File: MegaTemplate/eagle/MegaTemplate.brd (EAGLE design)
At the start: 160 x 100 mm, 7 parts

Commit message: Template for Arduino Mega Shields
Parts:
- moved SV6 52.5 mm to (30.5, 50.8)
- moved SV2 52.4 mm to (59.7, 2.54)
- moved SV3 44.4 mm to (82.5, 2.54)
- moved SV5 27.0 mm to (54.6, 50.8)
- moved SV7 18.3 mm to (95.2, 29.2), turned to 90 degrees
- moved SV4 13.7 mm to (77.5, 50.8)
- moved SV1 5.24 mm to (36.8, 2.54)
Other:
- board size 160 x 100 mm -> 101.6 x 53.3 mm

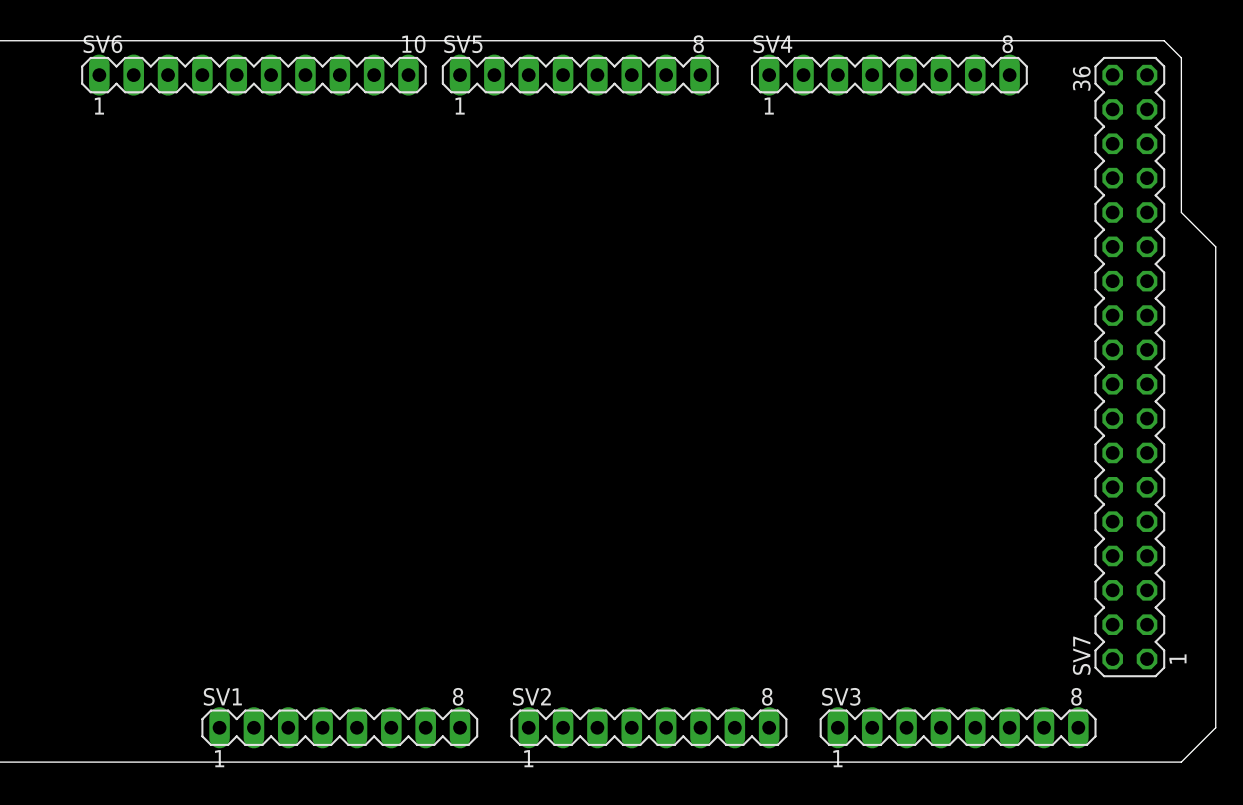
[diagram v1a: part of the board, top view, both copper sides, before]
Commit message: fixed pin header orientation
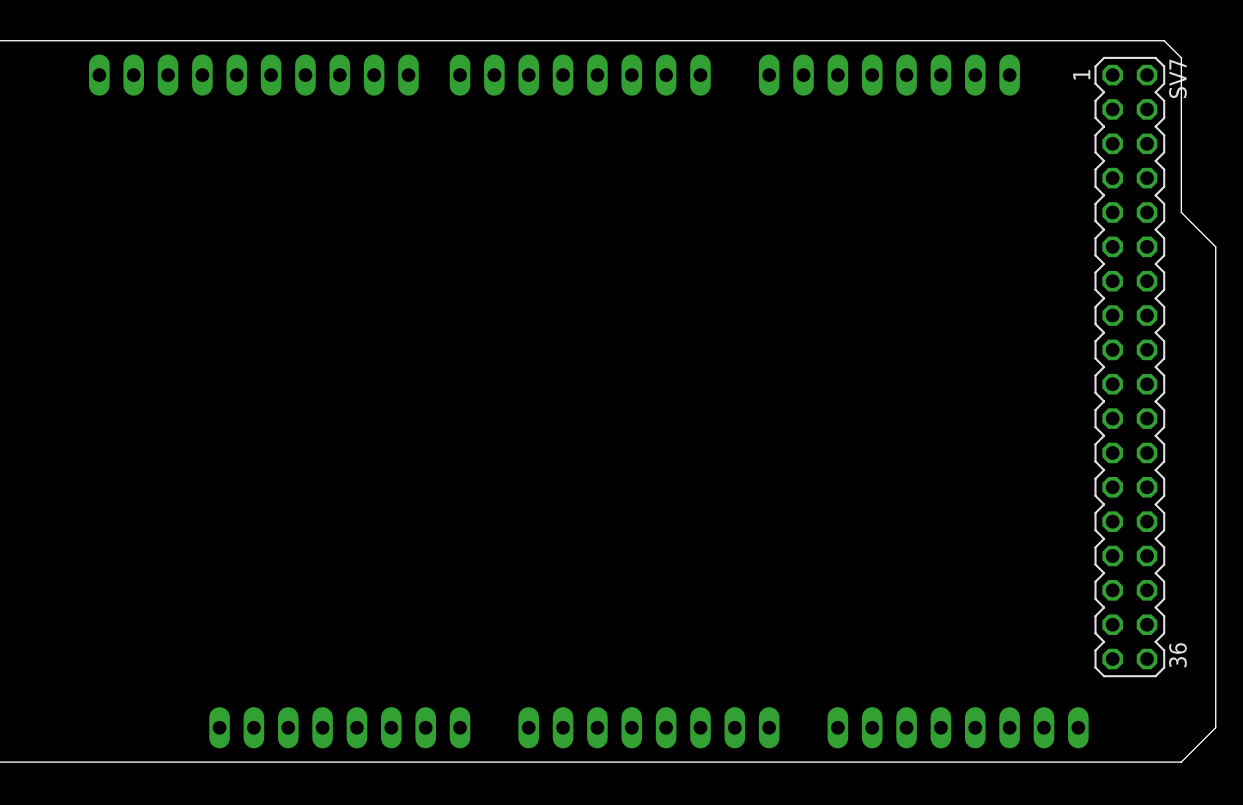
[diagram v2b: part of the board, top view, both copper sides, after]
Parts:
- flipped SV1 to the bottom
- flipped SV2 to the bottom
- flipped SV3 to the bottom
- flipped SV4 to the bottom
- flipped SV5 to the bottom
- flipped SV6 to the bottom
- turned SV7 to 270 degrees

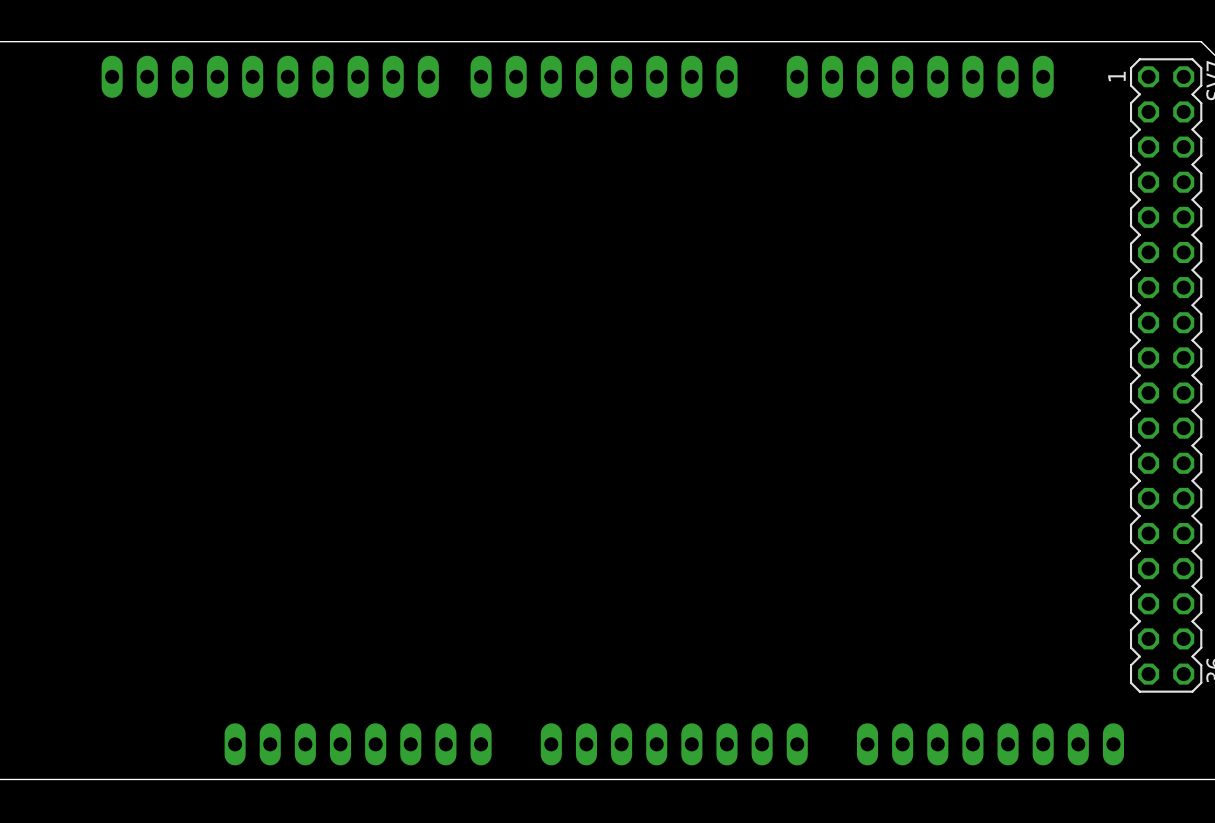
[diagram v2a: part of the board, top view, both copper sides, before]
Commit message: Ausrichtung vom Text gefixed
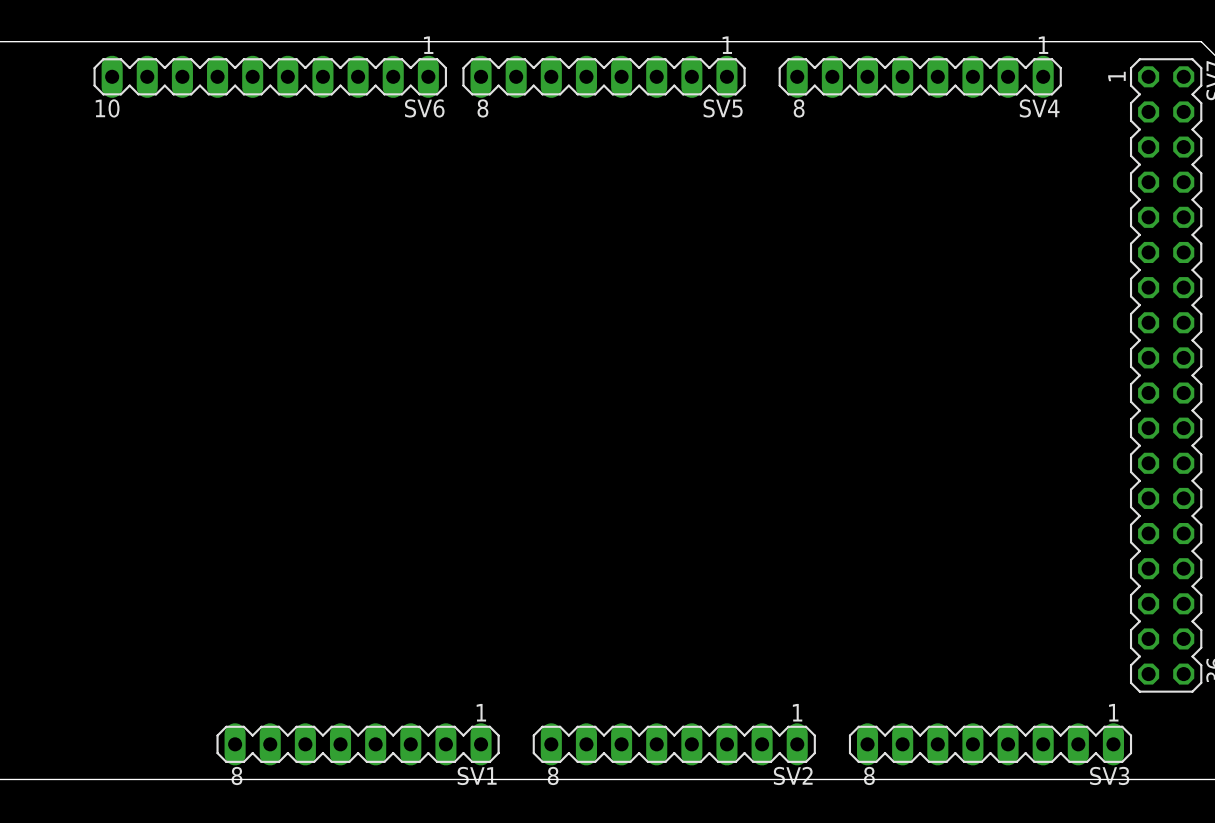
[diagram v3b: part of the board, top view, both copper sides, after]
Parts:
- flipped SV1 to the top, turned to 180 degrees
- flipped SV2 to the top, turned to 180 degrees
- flipped SV3 to the top, turned to 180 degrees
- flipped SV4 to the top, turned to 180 degrees
- flipped SV5 to the top, turned to 180 degrees
- flipped SV6 to the top, turned to 180 degrees
